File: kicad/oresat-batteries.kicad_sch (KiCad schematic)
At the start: 11 parts, among them J1 J-SAMTEC-TFM-120-X1-XXX-D-RA, SW1 Omron D2F-L3-D (LEFT), SW2 Omron D2F-L3-D (RIGHT), SW3 OMRON D2F-L3-D (LEFT), SW4 OMRON D2F-L3-D (RIGHT)

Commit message: Not sure what changed from back in February, but committing anyway :)
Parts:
- J1: DIS (none) -> DigiKey; DPN (none) -> SAM10145-ND
- PCB1: DIS (none) -> N/A; DPN (none) -> N/A; MFR (none) -> N/A; MPN (none) -> N/A; now left out of the parts list
- SW1: value Omron D2F-L3-D (LEFT) -> D2F-L3-D (LEFT); DIS (none) -> DigiKey; DPN (none) -> SW1443-ND; MFR (none) -> Oron Electronics; MPN (none) -> SW1443-ND
- SW2: value Omron D2F-L3-D (RIGHT) -> D2F-L3-D (RIGHT); DIS (none) -> DigiKey; DPN (none) -> SW1443-ND; MFR (none) -> Oron Electronics; MPN (none) -> SW1443-ND
- SW3: value OMRON D2F-L3-D (LEFT) -> D2F-L3-D (LEFT); DIS (none) -> DigiKey; DPN (none) -> SW1443-ND; MFR (none) -> Oron Electronics; MPN (none) -> SW1443-ND
- SW4: value OMRON D2F-L3-D (RIGHT) -> D2F-L3-D (RIGHT); DIS (none) -> DigiKey; DPN (none) -> SW1443-ND; MFR (none) -> Oron Electronics; MPN (none) -> SW1443-ND
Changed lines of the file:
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@@
 			)
 		)
-		(property "Value" "Omron D2F-L3-D (LEFT)"
+		(property "Value" "D2F-L3-D (LEFT)"
 			(at 194.31 247.65 0)
 			(effects
@@
 			)
 		)
-		(property "Datasheet" ""
+		(property "Datasheet" "https://mm.digikey.com/Volume0/opasdata/d220001/medias/docus/875/D2F_0318_DS.pdf"
 			(at 189.23 231.14 0)
 			(effects
@@
 			)
 		)
-		(property "Description" ""
+		(property "Description" "Switch SPDT Chassis Mount"
 			(at 189.23 231.14 0)
 			(effects
@@
 					(size 1.27 1.27)
 				)
+				(hide yes)
+			)
+		)
+		(property "DIS" "DigiKey"
+			(at 189.23 231.14 0)
+			(effects
+				(font
+					(size 1.27 1.27)
+				)
+				(hide yes)
+			)
+		)
+		(property "DPN" "SW1443-ND"
+			(at 189.23 231.14 0)
+			(effects
+				(font
+					(size 1.27 1.27)
+				)
+				(hide yes)
+			)
+		)
+		(property "MFR" "Oron Electronics"
+			(at 189.23 231.14 0)
+			(effects
+				(font
+					(size 1.27 1.27)
+				)
+				(hide yes)
+			)
+		)
+		(property "MPN" "SW1443-ND"
+			(at 189.23 231.14 0)
+			(effects
+				(font
+					(size 1.27 1.27)
+				)
+				(hide yes)
 			)
 		)
@@
 		(unit 1)
 		(exclude_from_sim no)
-		(in_bom yes)
+		(in_bom no)
 		(on_board yes)
 		(dnp no)
@@
 			)
 		)
-		(property "Datasheet" ""
+		(property "Datasheet" "N/A"
 			(at 63.5 218.44 0)
 			(effects
@@
 			)
 		)
-		(property "Description" ""
+		(property "Description" "N/A"
 			(at 63.5 218.44 0)
 			(effects
@@
 					(size 1.27 1.27)
 				)
+				(hide yes)
+			)
+		)
+		(property "DIS" "N/A"
+			(at 63.5 218.44 0)
+			(effects
+				(font
+					(size 1.27 1.27)
+				)
+				(hide yes)
+			)
+		)
+		(property "DPN" "N/A"
+			(at 63.5 218.44 0)
+			(effects
+				(font
+					(size 1.27 1.27)
+				)
+				(hide yes)
+			)
+		)
+		(property "MFR" "N/A"
+			(at 63.5 218.44 0)
+			(effects
+				(font
+					(size 1.27 1.27)
+				)
+				(hide yes)
+			)
+		)
+		(property "MPN" "N/A"
+			(at 63.5 218.44 0)
+			(effects
+				(font
+					(size 1.27 1.27)
+				)
+				(hide yes)
 			)
 		)
@@
 			)
 		)
-		(property "Value" "OMRON D2F-L3-D (LEFT)"
+		(property "Value" "D2F-L3-D (LEFT)"
 			(at 294.132 230.632 0)
 			(effects
@@
 			)
 		)
-		(property "Datasheet" ""
+		(property "Datasheet" "https://mm.digikey.com/Volume0/opasdata/d220001/medias/docus/875/D2F_0318_DS.pdf"
 			(at 294.64 223.52 0)
 			(effects
@@
 			)
 		)
-		(property "Description" ""
+		(property "Description" "Switch SPDT Chassis Mount"
 			(at 294.64 223.52 0)
 			(effects
@@
 					(size 1.27 1.27)
 				)
+				(hide yes)
+			)
+		)
+		(property "DIS" "DigiKey"
+			(at 294.64 223.52 0)
+			(effects
+				(font
+					(size 1.27 1.27)
+				)
+				(hide yes)
+			)
+		)
+		(property "DPN" "SW1443-ND"
+			(at 294.64 223.52 0)
+			(effects
+				(font
+					(size 1.27 1.27)
+				)
+				(hide yes)
+			)
+		)
+		(property "MFR" "Oron Electronics"
+			(at 294.64 223.52 0)
+			(effects
+				(font
+					(size 1.27 1.27)
+				)
+				(hide yes)
+			)
+		)
+		(property "MPN" "SW1443-ND"
+			(at 294.64 223.52 0)
+			(effects
+				(font
+					(size 1.27 1.27)
+				)
+				(hide yes)
 			)
 		)
@@
 			)
 		)
-		(property "Value" "OMRON D2F-L3-D (RIGHT)"
+		(property "Value" "D2F-L3-D (RIGHT)"
 			(at 250.19 228.6 0)
 			(effects
@@
 			)
 		)
-		(property "Datasheet" ""
+		(property "Datasheet" "https://mm.digikey.com/Volume0/opasdata/d220001/medias/docus/875/D2F_0318_DS.pdf"
 			(at 262.89 223.52 0)
 			(effects
@@
 			)
 		)
-		(property "Description" ""
+		(property "Description" "Switch SPDT Chassis Mount"
 			(at 262.89 223.52 0)
 			(effects
@@
 					(size 1.27 1.27)
 				)
+				(hide yes)
+			)
+		)
+		(property "DIS" "DigiKey"
+			(at 262.89 223.52 0)
+			(effects
+				(font
+					(size 1.27 1.27)
+				)
+				(hide yes)
+			)
+		)
+		(property "DPN" "SW1443-ND"
+			(at 262.89 223.52 0)
+			(effects
+				(font
+					(size 1.27 1.27)
+				)
+				(hide yes)
+			)
+		)
+		(property "MFR" "Oron Electronics"
+			(at 262.89 223.52 0)
+			(effects
+				(font
+					(size 1.27 1.27)
+				)
+				(hide yes)
+			)
+		)
+		(property "MPN" "SW1443-ND"
+			(at 262.89 223.52 0)
+			(effects
+				(font
+					(size 1.27 1.27)
+				)
+				(hide yes)
 			)
 		)
@@
 			)
 		)
-		(property "Datasheet" "https://suddendocs.samtec.com/catalog_english/tfm.pdf"
+		(property "Datasheet" "https://mm.digikey.com/Volume0/opasdata/d220001/medias/docus/6129/tfm-1xx-xx-xxx-d-xxx-x-xx-mkt.pdf"
 			(at 128.27 31.75 0)
 			(effects
@@
 			)
 		)
-		(property "Description" ""
+		(property "Description" "Connector Header Through Hole, Right Angle 40 position 0.050\" (1.27mm)"
 			(at 128.27 92.71 0)
 			(effects
@@
 					(size 1.27 1.27)
 				)
+				(hide yes)
 			)
 		)
@@
 				)
 				(justify left bottom)
+				(hide yes)
+			)
+		)
+		(property "DIS" "DigiKey"
+			(at 128.27 92.71 0)
+			(effects
+				(font
+					(size 1.27 1.27)
+				)
+				(hide yes)
+			)
+		)
+		(property "DPN" "SAM10145-ND"
+			(at 128.27 92.71 0)
+			(effects
+				(font
+					(size 1.27 1.27)
+				)
 				(hide yes)
 			)
@@
 			)
 		)
-		(property "Value" "Omron D2F-L3-D (RIGHT)"
+		(property "Value" "D2F-L3-D (RIGHT)"
 			(at 215.9 247.65 0)
 			(effects
@@
 			)
 		)
-		(property "Datasheet" ""
+		(property "Datasheet" "https://mm.digikey.com/Volume0/opasdata/d220001/medias/docus/875/D2F_0318_DS.pdf"
 			(at 210.82 231.14 0)
 			(effects
@@
 			)
 		)
-		(property "Description" ""
+		(property "Description" "Switch SPDT Chassis Mount"
 			(at 210.82 231.14 0)
 			(effects
@@
 					(size 1.27 1.27)
 				)
-			)
-		)
+				(hide yes)
+			)
+		)
+		(property "DIS" "DigiKey"
+			(at 210.82 231.14 0)
+			(effects
+				(font
+					(size 1.27 1.27)
+				)
+				(hide yes)
+			)
+		)
+		(property "DPN" "SW1443-ND"
+			(at 210.82 231.14 0)
+			(effects
+				(font
+					(size 1.27 1.27)
+				)
+				(hide yes)
+			)
+		)
+		(property "MFR" "Oron Electronics"
+			(at 210.82 231.14 0)
+			(effects
+				(font
+					(size 1.27 1.27)
+				)
+				(hide yes)
+			)
+		)
+		(property "MPN" "SW1443-ND"
+			(at 210.82 231.14 0)
+			(effects
+				(font
+					(size 1.27 1.27)
+				)
+				(hide yes)
+			)
+		)

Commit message: Updated data, spiffed up the root page, renamed some STM specific OPD signals, synced SCH and BRD, fixed a bunch of DRC errors, NOW ready for MCXN import that will screw everything up.
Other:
- sheet Power renamed OreSat Power Domain (OPD)
- sheet Battery Pack 1 (BOTTOM) ports: added I2C1_SCL, I2C1_SDA; removed PB6/SCL, PB7/SDA
- sheet Microcontroller ports: added I2C1_SCL, I2C1_SDA, MCU-UART-RX, MCU-UART-TX; removed PA2/USART2_TX, PA3/USART2_RX, PB6/SCL, PB7/SDA
- sheet OreSat Power Domain (OPD) ports: added MCU-UART-RX, MCU-UART-TX; removed PA2/USART2_TX, PA3/USART2_RX
- moved on the sheet: J1, SW1, SW2, SW3, SW4, TP25, TP57

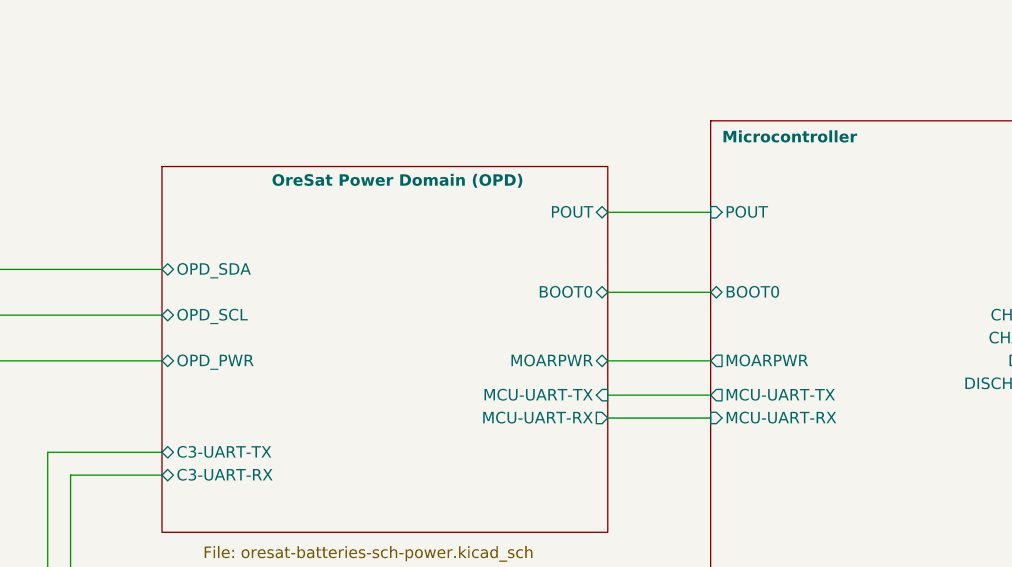
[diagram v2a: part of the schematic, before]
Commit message: Added MCXN. Preliminary power layout, started removal of old symbols and footprints.
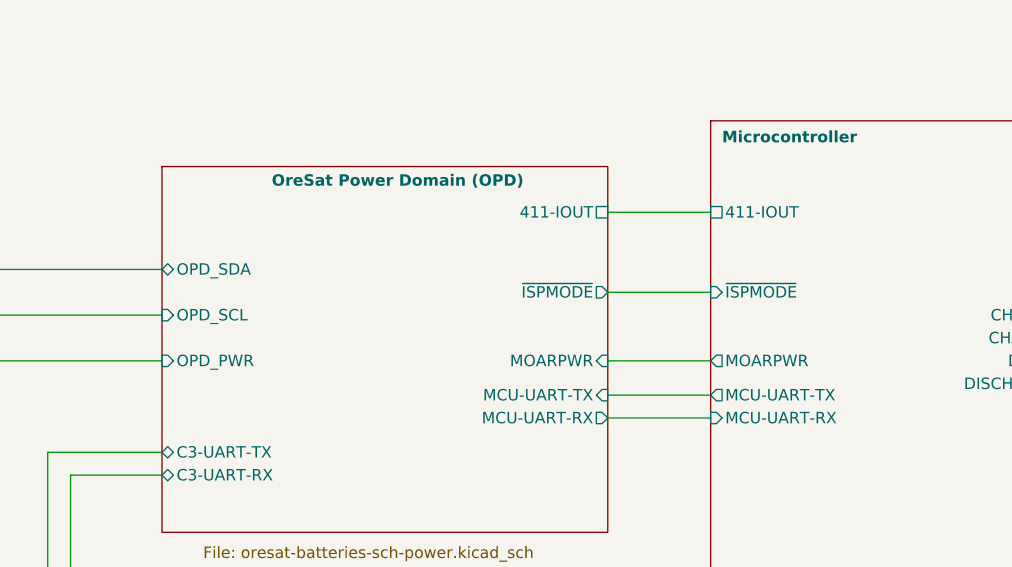
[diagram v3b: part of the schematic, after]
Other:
- sheet Microcontroller ports: added 411-IOUT, ~{ISPMODE}; removed BOOT0, POUT
- sheet OreSat Power Domain (OPD) ports: added 411-IOUT, ~{ISPMODE}; removed BOOT0, POUT
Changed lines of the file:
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@@
 			)
 		)
-		(pin "BOOT0" bidirectional
+		(pin "~{ISPMODE}" input
 			(at 213.36 58.42 180)
 			(effects
@@
 			)
 		)
-		(pin "POUT" input
+		(pin "411-IOUT" passive
 			(at 213.36 49.53 180)
 			(effects
@@
 			)
 		)
-		(pin "OPD_PWR" bidirectional
+		(pin "OPD_PWR" input
 			(at 152.4 66.04 180)
 			(effects
@@
 			)
 		)
-		(pin "OPD_SCL" bidirectional
+		(pin "OPD_SCL" input
 			(at 152.4 60.96 180)
 			(effects
@@
 			)
 		)
-		(pin "BOOT0" bidirectional
+		(pin "~{ISPMODE}" output
 			(at 201.93 58.42 0)
 			(effects
@@
 			)
 		)
-		(pin "MOARPWR" bidirectional
+		(pin "MOARPWR" input
 			(at 201.93 66.04 0)
 			(effects
@@
 			)
 		)
-		(pin "POUT" bidirectional
+		(pin "411-IOUT" passive
 			(at 201.93 49.53 0)
 			(effects

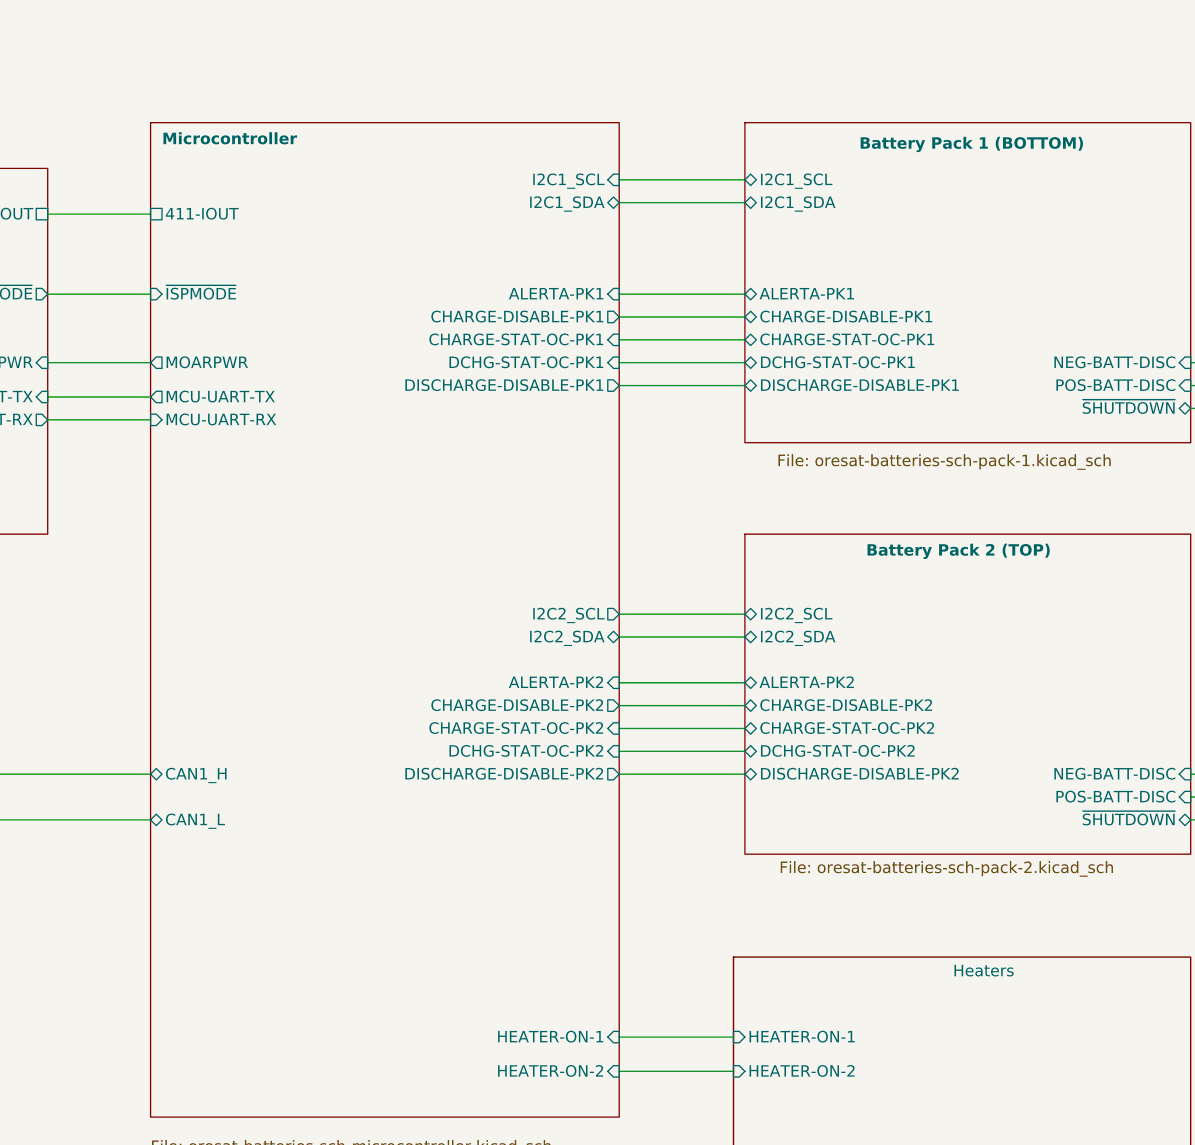
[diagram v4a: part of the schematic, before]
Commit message: Schematic complete with new TPS circuit breaker; layout in progress
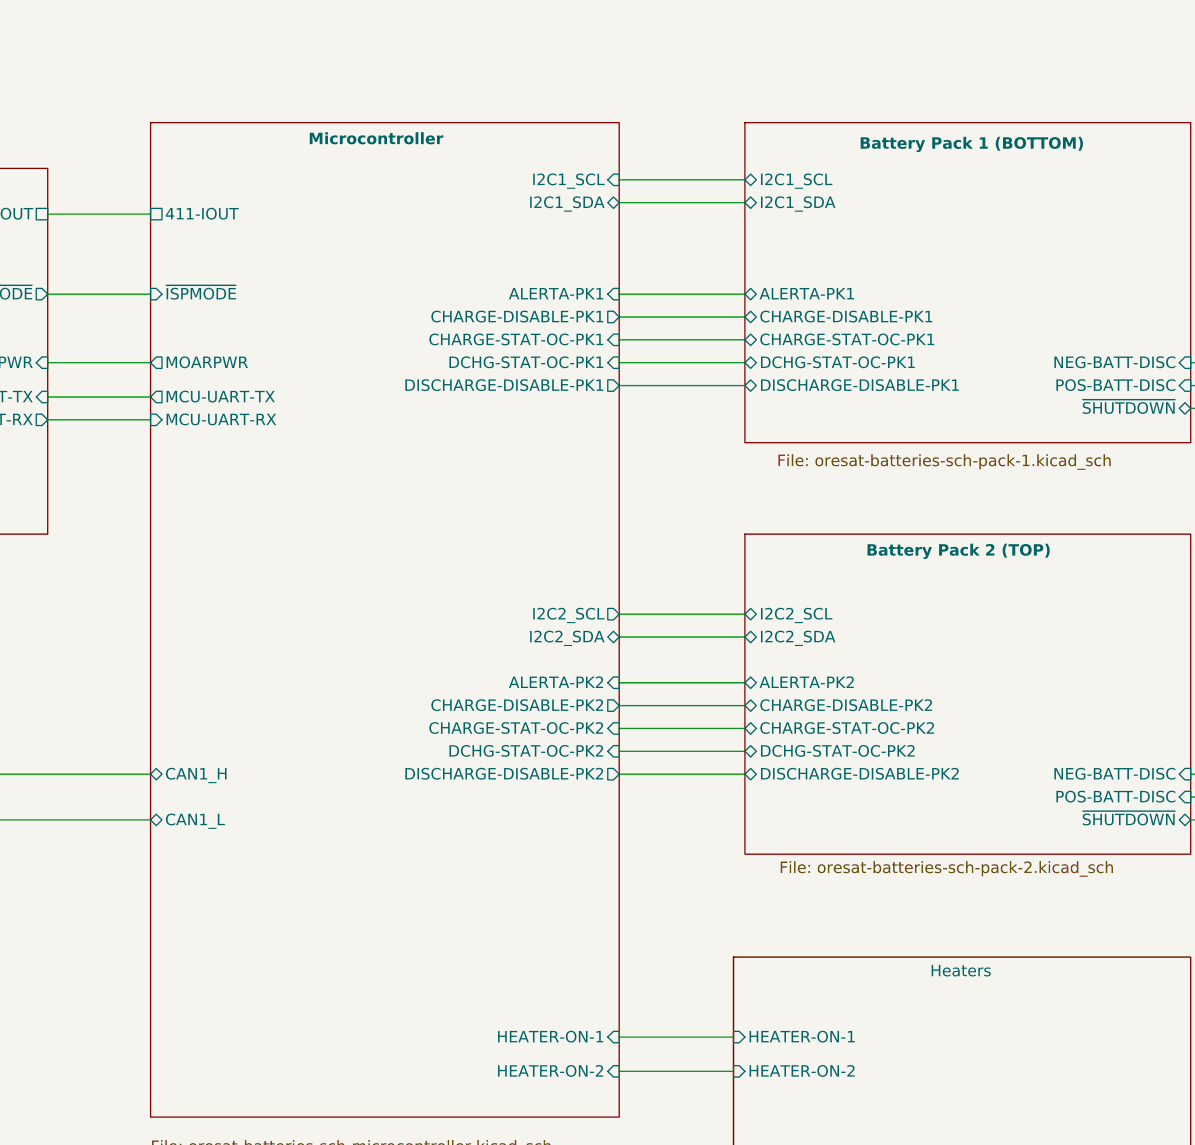
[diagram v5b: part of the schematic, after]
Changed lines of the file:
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@@
 		)
 		(property "Sheetname" "Microcontroller"
-			(at 214.63 41.91 0)
+			(at 230.886 41.91 0)
 			(show_name no)
 			(do_not_autoplace no)
@@
 		)
 		(property "Sheetname" "Heaters"
-			(at 302.514 134.366 0)
+			(at 299.974 134.366 0)
 			(show_name no)
 			(do_not_autoplace no)
